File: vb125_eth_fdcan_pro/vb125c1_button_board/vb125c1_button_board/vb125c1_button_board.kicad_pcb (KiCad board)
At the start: 2 copper layers, 27.3 x 15.2 mm, 3 parts, among them SW1 KSS331GLFS

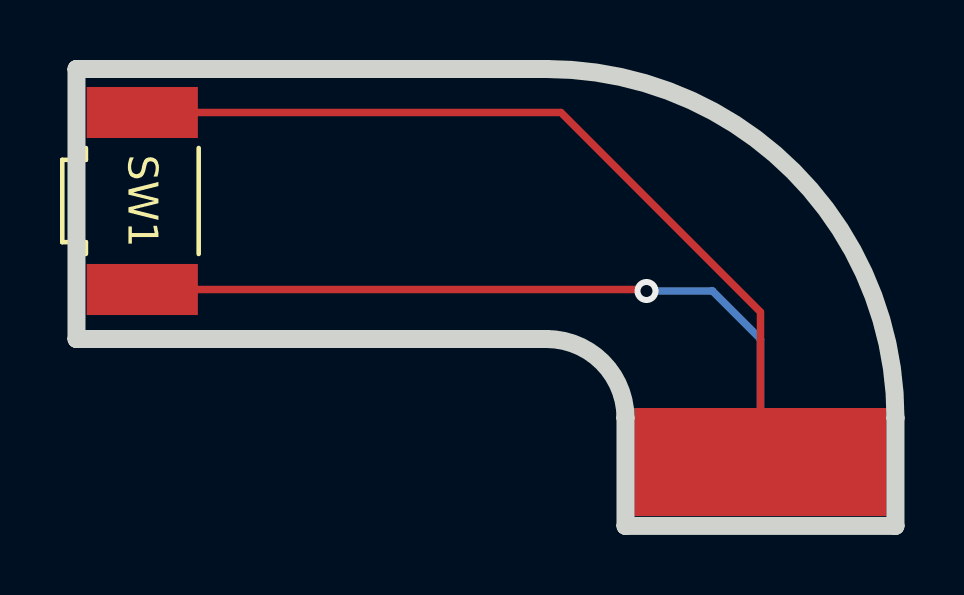
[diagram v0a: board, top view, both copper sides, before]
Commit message: Update PCB outline.
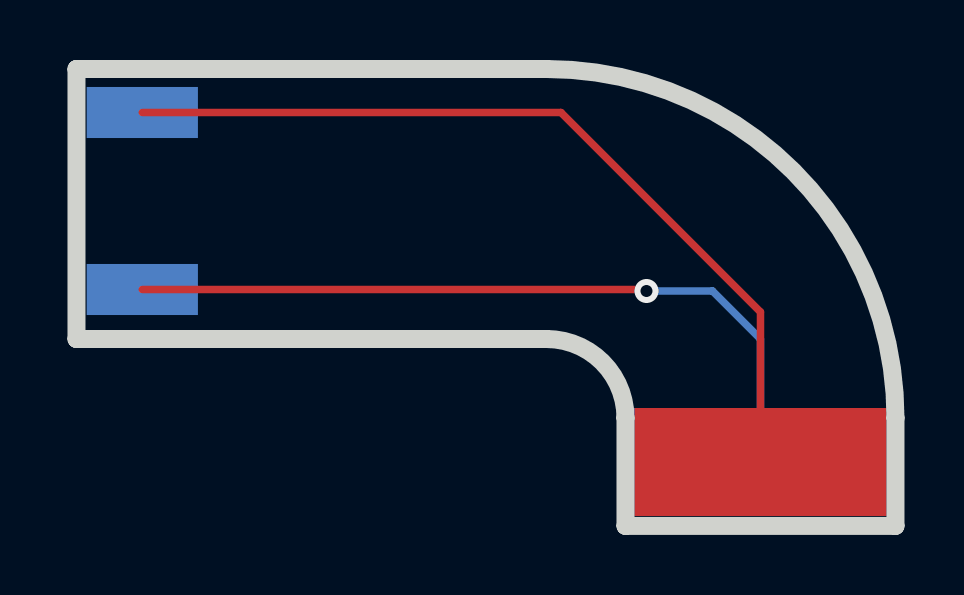
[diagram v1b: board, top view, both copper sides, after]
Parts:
- SW1: moved to B.Cu
- turned SW1 to 90 degrees
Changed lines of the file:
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@@
   (net 1 "Net-(SW1-Pad1)")
   (net 2 "Net-(SW1-Pad2)")
-  (footprint "vhrd_electromechanical:SW_KSS3" (layer "F.Cu")
-    (at -16.106246 -10.830135 -90)
-    (tags "KSS331GLFS ")
-    (property "Sheetfile" "vb125c1_button_board.kicad_sch")
-    (property "Sheetname" "")
-    (property "ki_description" "Push button switch, generic, two pins")
-    (property "ki_keywords" "switch normally-open pushbutton push-button")
-    (attr smd)
-    (fp_text reference "SW1" (at 0 0 -90 unlocked) (layer "F.SilkS")
-        (effects (font (size 1 1) (thickness 0.15)))
-    )
-    (fp_text value "KSS331GLFS" (at 0 0 -90 unlocked) (layer "F.Fab")
-        (effects (font (size 1 1) (thickness 0.15)))
-    )
-    (fp_text user "${REFERENCE}" (at 0 0 -90 unlocked) (layer "F.Fab")
-        (effects (font (size 1 1) (thickness 0.15)))
-    )
-    (fp_line (start -1.76733 1.8796) (end -1.3716 1.8796)
-      (stroke (width 0.1524) (type solid)) (layer "F.SilkS"))
-    (fp_line (start -1.3716 1.8796) (end -1.3716 2.667)
-      (stroke (width 0.1524) (type solid)) (layer "F.SilkS"))
-    (fp_line (start -1.3716 2.667) (end 1.3716 2.667)
-      (stroke (width 0.1524) (type solid)) (layer "F.SilkS"))
-    (fp_line (start 1.3716 1.8796) (end 1.76733 1.8796)
-      (stroke (width 0.1524) (type solid)) (layer "F.SilkS"))
-    (fp_line (start 1.3716 2.667) (end 1.3716 1.8796)
-      (stroke (width 0.1524) (type solid)) (layer "F.SilkS"))
-    (fp_line (start 1.76733 -1.8796) (end -1.76733 -1.8796)
-      (stroke (width 0.1524) (type solid)) (layer "F.SilkS"))
-    (fp_line (start -4.0132 -2.0066) (end -4.0132 2.0066)
-      (stroke (width 0.1524) (type solid)) (layer "F.CrtYd"))
-    (fp_line (start -4.0132 2.0066) (end -1.4986 2.0066)
-      (stroke (width 0.1524) (type solid)) (layer "F.CrtYd"))
-    (fp_line (start -1.4986 2.0066) (end -1.4986 2.794)
-      (stroke (width 0.1524) (type solid)) (layer "F.CrtYd"))
-    (fp_line (start -1.4986 2.794) (end 1.4986 2.794)
-      (stroke (width 0.1524) (type solid)) (layer "F.CrtYd"))
-    (fp_line (start 1.4986 2.0066) (end 4.0132 2.0066)
-      (stroke (width 0.1524) (type solid)) (layer "F.CrtYd"))
-    (fp_line (start 1.4986 2.794) (end 1.4986 2.0066)
-      (stroke (width 0.1524) (type solid)) (layer "F.CrtYd"))
-    (fp_line (start 4.0132 -2.0066) (end -4.0132 -2.0066)
-      (stroke (width 0.1524) (type solid)) (layer "F.CrtYd"))
-    (fp_line (start 4.0132 2.0066) (end 4.0132 -2.0066)
-      (stroke (width 0.1524) (type solid)) (layer "F.CrtYd"))
-    (fp_line (start -3.5052 -1.7526) (end -3.5052 1.7526)
-      (stroke (width 0.0254) (type solid)) (layer "F.Fab"))
-    (fp_line (start -3.5052 1.7526) (end 3.5052 1.7526)
-      (stroke (width 0.0254) (type solid)) (layer "F.Fab"))
-    (fp_line (start -1.2446 1.7526) (end -1.2446 2.5654)
-      (stroke (width 0.0254) (type solid)) (layer "F.Fab"))
-    (fp_line (start -1.2446 2.5654) (end 1.2446 2.5654)
-      (stroke (width 0.0254) (type solid)) (layer "F.Fab"))
-    (fp_line (start 1.2446 2.5654) (end 1.2446 1.7526)
-      (stroke (width 0.0254) (type solid)) (layer "F.Fab"))
-    (fp_line (start 3.5052 -1.7526) (end -3.5052 -1.7526)
-      (stroke (width 0.0254) (type solid)) (layer "F.Fab"))
-    (fp_line (start 3.5052 1.7526) (end 3.5052 -1.7526)
-      (stroke (width 0.0254) (type solid)) (layer "F.Fab"))
-    (fp_arc (start 0.3048 -1.7526) (mid 0 -1.4478) (end -0.3048 -1.7526)
-      (stroke (width 0.0254) (type solid)) (layer "F.Fab"))
-    (fp_circle (center -1.9304 -0.889) (end -1.8923 -0.889)
-      (stroke (width 0.0254) (type solid)) (fill none) (layer "F.Fab"))
-    (pad "1" smd rect (at -2.949999 0 270) (size 1.7018 3.7084) (layers "F.Cu" "F.Paste" "F.Mask")
-      (net 1 "Net-(SW1-Pad1)") (pinfunction "1") (pintype "passive"))
-    (pad "2" smd rect (at 2.949999 0 270) (size 1.7018 3.7084) (layers "F.Cu" "F.Paste" "F.Mask")
-      (net 2 "Net-(SW1-Pad2)") (pinfunction "2") (pintype "passive"))
-    (model "${VHRD_3DMODEL_DIR}/electromechanical/button/KSS331.STEP"
-      (offset (xyz 0 0 0))
-      (scale (xyz 1 1 1))
-      (rotate (xyz 0 0 180))
-    )
-  )
   (footprint "TestPoint:TestPoint_Pad_4.0x4.0mm" (layer "F.Cu")
     (at 4.500054 -2.130135)
@@
       (net 1 "Net-(SW1-Pad1)") (pinfunction "1") (pintype "passive"))
   )
+  (footprint "vhrd_electromechanical:SW_KSS3" (layer "B.Cu")
+    (at -16.106246 -10.830135 90)
+    (tags "KSS331GLFS ")
+    (property "Sheetfile" "vb125c1_button_board.kicad_sch")
+    (property "Sheetname" "")
+    (property "ki_description" "Push button switch, generic, two pins")
+    (property "ki_keywords" "switch normally-open pushbutton push-button")
+    (attr smd)
+    (fp_text reference "SW1" (at 0 0 270 unlocked) (layer "B.SilkS")
+        (effects (font (size 1 1) (thickness 0.15)) (justify mirror))
+    )
+    (fp_text value "KSS331GLFS" (at 0 0 270 unlocked) (layer "B.Fab")
+        (effects (font (size 1 1) (thickness 0.15)) (justify mirror))
+    )
+    (fp_text user "${REFERENCE}" (at 0 0 270 unlocked) (layer "B.Fab")
+        (effects (font (size 1 1) (thickness 0.15)) (justify mirror))
+    )
+    (fp_line (start -1.76733 -1.8796) (end -1.3716 -1.8796)
+      (stroke (width 0.1524) (type solid)) (layer "B.SilkS"))
+    (fp_line (start -1.3716 -2.667) (end 1.3716 -2.667)
+      (stroke (width 0.1524) (type solid)) (layer "B.SilkS"))
+    (fp_line (start -1.3716 -1.8796) (end -1.3716 -2.667)
+      (stroke (width 0.1524) (type solid)) (layer "B.SilkS"))
+    (fp_line (start 1.3716 -2.667) (end 1.3716 -1.8796)
+      (stroke (width 0.1524) (type solid)) (layer "B.SilkS"))
+    (fp_line (start 1.3716 -1.8796) (end 1.76733 -1.8796)
+      (stroke (width 0.1524) (type solid)) (layer "B.SilkS"))
+    (fp_line (start 1.76733 1.8796) (end -1.76733 1.8796)
+      (stroke (width 0.1524) (type solid)) (layer "B.SilkS"))
+    (fp_line (start -4.0132 -2.0066) (end -1.4986 -2.0066)
+      (stroke (width 0.1524) (type solid)) (layer "B.CrtYd"))
+    (fp_line (start -4.0132 2.0066) (end -4.0132 -2.0066)
+      (stroke (width 0.1524) (type solid)) (layer "B.CrtYd"))
+    (fp_line (start -1.4986 -2.794) (end 1.4986 -2.794)
+      (stroke (width 0.1524) (type solid)) (layer "B.CrtYd"))
+    (fp_line (start -1.4986 -2.0066) (end -1.4986 -2.794)
+      (stroke (width 0.1524) (type solid)) (layer "B.CrtYd"))
+    (fp_line (start 1.4986 -2.794) (end 1.4986 -2.0066)
+      (stroke (width 0.1524) (type solid)) (layer "B.CrtYd"))
+    (fp_line (start 1.4986 -2.0066) (end 4.0132 -2.0066)
+      (stroke (width 0.1524) (type solid)) (layer "B.CrtYd"))
+    (fp_line (start 4.0132 -2.0066) (end 4.0132 2.0066)
+      (stroke (width 0.1524) (type solid)) (layer "B.CrtYd"))
+    (fp_line (start 4.0132 2.0066) (end -4.0132 2.0066)
+      (stroke (width 0.1524) (type solid)) (layer "B.CrtYd"))
+    (fp_line (start -3.5052 -1.7526) (end 3.5052 -1.7526)
+      (stroke (width 0.0254) (type solid)) (layer "B.Fab"))
+    (fp_line (start -3.5052 1.7526) (end -3.5052 -1.7526)
+      (stroke (width 0.0254) (type solid)) (layer "B.Fab"))
+    (fp_line (start -1.2446 -2.5654) (end 1.2446 -2.5654)
+      (stroke (width 0.0254) (type solid)) (layer "B.Fab"))
+    (fp_line (start -1.2446 -1.7526) (end -1.2446 -2.5654)
+      (stroke (width 0.0254) (type solid)) (layer "B.Fab"))
+    (fp_line (start 1.2446 -2.5654) (end 1.2446 -1.7526)
+      (stroke (width 0.0254) (type solid)) (layer "B.Fab"))
+    (fp_line (start 3.5052 -1.7526) (end 3.5052 1.7526)
+      (stroke (width 0.0254) (type solid)) (layer "B.Fab"))
+    (fp_line (start 3.5052 1.7526) (end -3.5052 1.7526)
+      (stroke (width 0.0254) (type solid)) (layer "B.Fab"))
+    (fp_arc (start -0.3048 1.7526) (mid 0 1.4478) (end 0.3048 1.7526)
+      (stroke (width 0.0254) (type solid)) (layer "B.Fab"))
+    (fp_circle (center -1.9304 0.889) (end -1.8923 0.889)
+      (stroke (width 0.0254) (type solid)) (fill none) (layer "B.Fab"))
+    (pad "1" smd rect (at -2.949999 0 90) (size 1.7018 3.7084) (layers "B.Cu" "B.Paste" "B.Mask")
+      (net 1 "Net-(SW1-Pad1)") (pinfunction "1") (pintype "passive"))
+    (pad "2" smd rect (at 2.949999 0 90) (size 1.7018 3.7084) (layers "B.Cu" "B.Paste" "B.Mask")
+      (net 2 "Net-(SW1-Pad2)") (pinfunction "2") (pintype "passive"))
+    (model "${VHRD_3DMODEL_DIR}/electromechanical/button/KSS331.STEP"
+      (offset (xyz 0 0 0))
+      (scale (xyz 1 1 1))
+      (rotate (xyz 0 0 180))
+    )
+  )
   (footprint "TestPoint:TestPoint_Pad_4.0x4.0mm" (layer "B.Cu")
